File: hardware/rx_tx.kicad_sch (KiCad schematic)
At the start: 13 parts, among them J3 SMA_Conn, U4 MIC5317-3.0YD5-TR, U5 MAX41462GUB+, Y1 ECS-160-12-37B-CTN-TR

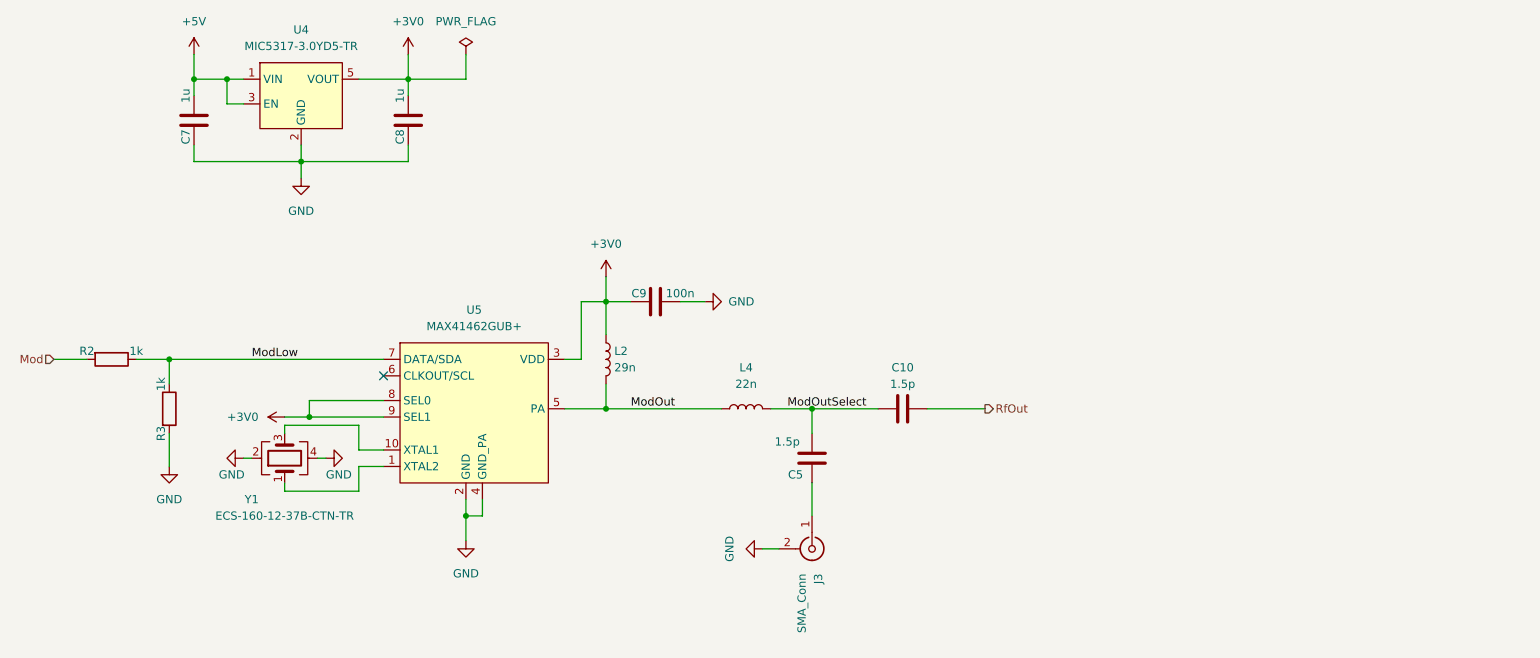
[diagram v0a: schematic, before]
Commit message: splitted quad opamp into dual opamp and comparator for better digitalization and smaller board
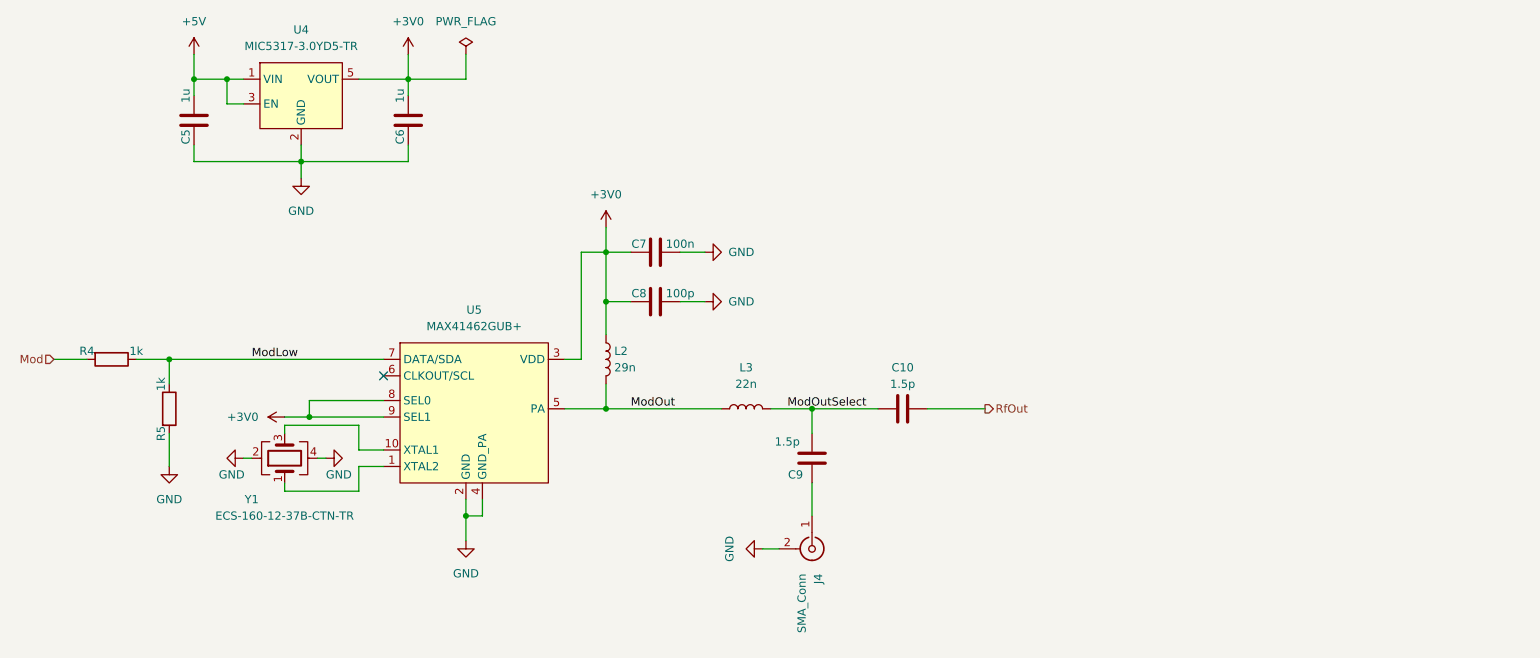
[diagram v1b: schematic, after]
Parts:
- added C8: 100p, Capacitor_SMD:C_0603_1608Metric, symbol Device:C
- renumbered C7 to C5, C8 to C6, C9 to C7, C5 to C9, J3 to J4, L4 to L3, R2 to R4, R3 to R5
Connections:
- net +3V0: now also C8.2
- net GND: now also C8.1
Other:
- moved on the sheet: C7

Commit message: added PA and changed directional coupler
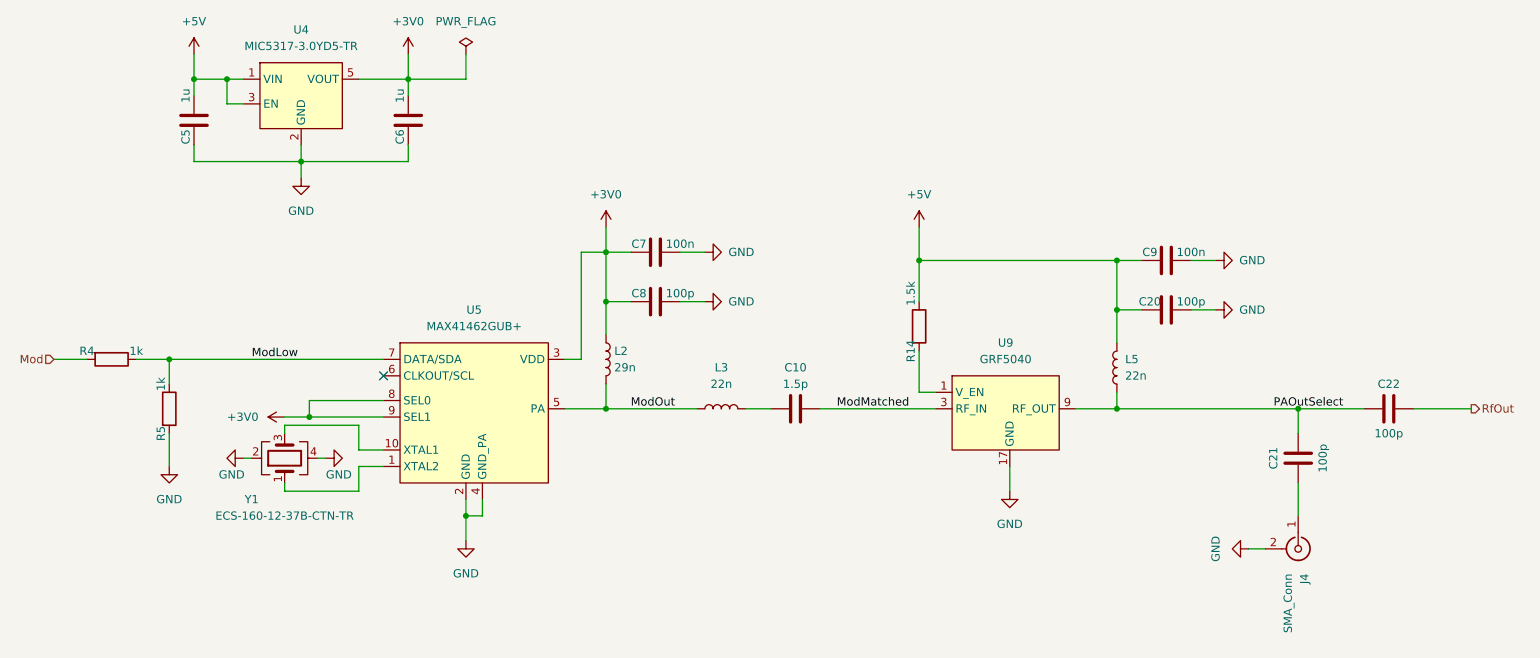
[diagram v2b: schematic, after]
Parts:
- added C20, C21, C22: 100p, Capacitor_SMD:C_0603_1608Metric, symbol Device:C
- added L5: 22n, Inductor_SMD:L_0603_1608Metric, symbol Device:L
- added R14: 1.5k, Resistor_SMD:R_0603_1608Metric, symbol Device:R
- added U9: GRF5040, Package_DFN_QFN:QFN-16-1EP_3x3mm_P0.5mm_EP1.7x1.7mm, symbol ProjLib:GRF5040
- C9: value 1.5p -> 100n; now in the parts list
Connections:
- net +5V: now also C9.1, C20.2, L5.2, R14.1
- net GND: now also C9.2, C20.1, U9.11 (GND), U9.12 (GND), U9.13 (GND), U9.14 (GND), U9.15 (GND), U9.16 (GND), U9.17 (GND), U9.2 (GND), U9.5 (GND), U9.6 (GND), U9.7 (GND), U9.8 (GND)
- net RfOut: now also C22.1; no longer C10.1
- net at J4.1 (In): now also C21.2; no longer C9.2
- net ModOutSelect: no longer names the net of C10.2, L3.2
- net ModOutSelect: no longer C9.1
- new net: R14.2, U9.1 (V_EN)
- new net ModMatched: C10.1, U9.3 (RF_IN), U9.4 (RF_IN)
- new net PAOutSelect: C21.1, C22.2, L5.1, U9.10 (RF_OUT), U9.9 (RF_OUT)
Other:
- moved on the sheet: C10, J4, L3
